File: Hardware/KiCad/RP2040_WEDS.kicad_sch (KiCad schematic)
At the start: 75 parts, among them J1 Barrel_Jack_Switch_Pin3Ring, J2 Conn_01x02_Male, J3 I2C Soil Header, J4 LiPo Batt, J5 Analog Soil Header, J6 USB Header, J7 Conn_02x05_Odd_Even, J8 SMA-J-P-H-RA-TH1, Q1 Q_PMOS_DGS, Q2 Q_PMOS_DGS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

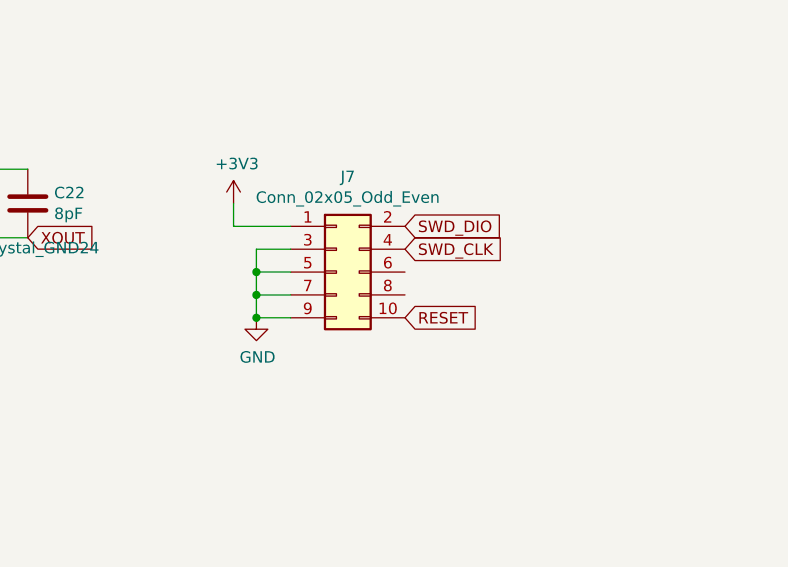
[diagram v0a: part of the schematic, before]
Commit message: added thermal relief to fill zones
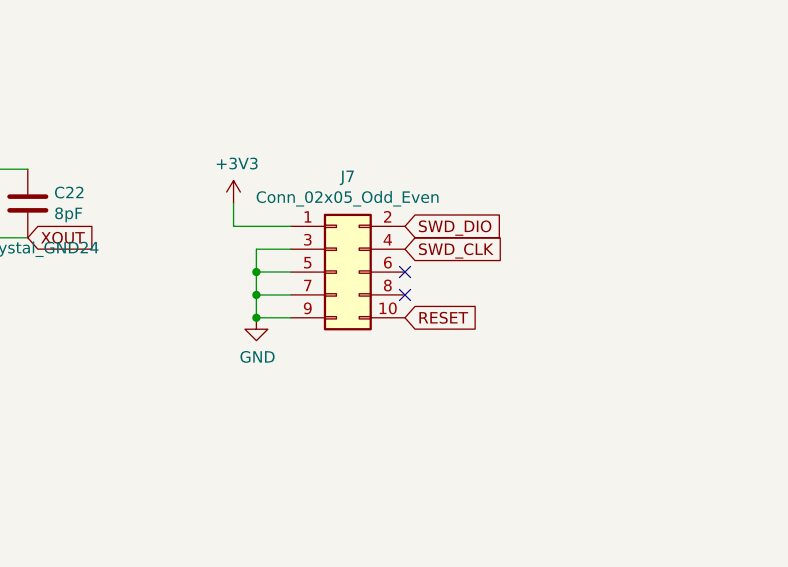
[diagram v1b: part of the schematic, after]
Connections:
- no-connect marks 41 -> 43
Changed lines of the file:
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@@
   (no_connect (at 35.56 149.86))
   (no_connect (at 81.28 134.62))
+  (no_connect (at 266.7 153.67))
+  (no_connect (at 266.7 151.13))
   (no_connect (at 228.6 77.47))
   (no_connect (at 223.52 77.47))

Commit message: changed the size of headers form 1.27 to 2.54mm
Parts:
- J2: footprint Connector_PinHeader_1.27mm:PinHeader_1x02_P1.27mm_Vertical -> Connector_PinSocket_2.54mm:PinSocket_1x02_P2.54mm_Vertical
- J3: footprint Connector_PinHeader_1.27mm:PinHeader_1x04_P1.27mm_Vertical -> Connector_PinHeader_2.54mm:PinHeader_1x04_P2.54mm_Horizontal
- J4: footprint Connector_PinHeader_1.27mm:PinHeader_2x01_P1.27mm_Vertical -> Connector_PinHeader_2.54mm:PinHeader_2x01_P2.54mm_Vertical
- J5: footprint Connector_PinHeader_1.27mm:PinHeader_1x03_P1.27mm_Vertical -> Connector_PinHeader_2.54mm:PinHeader_1x03_P2.54mm_Horizontal
- J6: footprint Connector_PinHeader_1.27mm:PinHeader_1x04_P1.27mm_Vertical -> Connector_PinHeader_2.54mm:PinHeader_1x04_P2.54mm_Vertical
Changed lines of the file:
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@@
       (effects (font (size 1.27 1.27)) (justify left))
     )
-    (property "Footprint" "Connector_PinHeader_1.27mm:PinHeader_2x01_P1.27mm_Vertical" (id 2) (at 106.68 54.61 0)
+    (property "Footprint" "Connector_PinHeader_2.54mm:PinHeader_2x01_P2.54mm_Vertical" (id 2) (at 106.68 54.61 0)
       (effects (font (size 1.27 1.27)) hide)
     )
@@
     (property "Reference" "J5" (id 0) (at 138.6332 122.4026 0))
     (property "Value" "Analog Soil Header" (id 1) (at 138.6332 124.714 0))
-    (property "Footprint" "Connector_PinHeader_1.27mm:PinHeader_1x03_P1.27mm_Vertical" (id 2) (at 135.89 129.54 0)
+    (property "Footprint" "Connector_PinHeader_2.54mm:PinHeader_1x03_P2.54mm_Horizontal" (id 2) (at 135.89 129.54 0)
       (effects (font (size 1.27 1.27)) hide)
     )
@@
     (property "Reference" "J3" (id 0) (at 108.1532 122.4026 0))
     (property "Value" "I2C Soil Header" (id 1) (at 108.1532 124.714 0))
-    (property "Footprint" "Connector_PinHeader_1.27mm:PinHeader_1x04_P1.27mm_Vertical" (id 2) (at 105.41 129.54 0)
+    (property "Footprint" "Connector_PinHeader_2.54mm:PinHeader_1x04_P2.54mm_Horizontal" (id 2) (at 105.41 129.54 0)
       (effects (font (size 1.27 1.27)) hide)
     )
@@
     (property "Reference" "J2" (id 0) (at 93.345 168.944 0))
     (property "Value" "Conn_01x02_Male" (id 1) (at 87.63 177.8 0))
-    (property "Footprint" "Connector_PinHeader_1.27mm:PinHeader_1x02_P1.27mm_Vertical" (id 2) (at 92.71 172.72 0)
+    (property "Footprint" "Connector_PinSocket_2.54mm:PinSocket_1x02_P2.54mm_Vertical" (id 2) (at 92.71 172.72 0)
       (effects (font (size 1.27 1.27)) hide)
     )
@@
     (property "Reference" "J6" (id 0) (at 169.545 121.92 0))
     (property "Value" "USB Header" (id 1) (at 169.545 124.46 0))
-    (property "Footprint" "Connector_PinHeader_1.27mm:PinHeader_1x04_P1.27mm_Vertical" (id 2) (at 168.91 129.54 0)
+    (property "Footprint" "Connector_PinHeader_2.54mm:PinHeader_1x04_P2.54mm_Vertical" (id 2) (at 168.91 129.54 0)
       (effects (font (size 1.27 1.27)) hide)
     )
@@
     )
     (path "/87f53324-fd34-468e-b98f-06d9b31382af"
-      (reference "J2") (unit 1) (value "Conn_01x02_Male") (footprint "Connector_PinHeader_1.27mm:PinHeader_1x02_P1.27mm_Vertical")
+      (reference "J2") (unit 1) (value "Conn_01x02_Male") (footprint "Connector_PinSocket_2.54mm:PinSocket_1x02_P2.54mm_Vertical")
     )
     (path "/00000000-0000-0000-0000-0000625e3cae"
-      (reference "J3") (unit 1) (value "I2C Soil Header") (footprint "Connector_PinHeader_1.27mm:PinHeader_1x04_P1.27mm_Vertical")
+      (reference "J3") (unit 1) (value "I2C Soil Header") (footprint "Connector_PinHeader_2.54mm:PinHeader_1x04_P2.54mm_Horizontal")
     )
     (path "/00000000-0000-0000-0000-00006209bd4a"
-      (reference "J4") (unit 1) (value "LiPo Batt") (footprint "Connector_PinHeader_1.27mm:PinHeader_2x01_P1.27mm_Vertical")
+      (reference "J4") (unit 1) (value "LiPo Batt") (footprint "Connector_PinHeader_2.54mm:PinHeader_2x01_P2.54mm_Vertical")
     )
     (path "/00000000-0000-0000-0000-0000625a9016"
-      (reference "J5") (unit 1) (value "Analog Soil Header") (footprint "Connector_PinHeader_1.27mm:PinHeader_1x03_P1.27mm_Vertical")
+      (reference "J5") (unit 1) (value "Analog Soil Header") (footprint "Connector_PinHeader_2.54mm:PinHeader_1x03_P2.54mm_Horizontal")
     )
     (path "/dc005aba-36e3-4558-88a0-257925ac0539"
-      (reference "J6") (unit 1) (value "USB Header") (footprint "Connector_PinHeader_1.27mm:PinHeader_1x04_P1.27mm_Vertical")
+      (reference "J6") (unit 1) (value "USB Header") (footprint "Connector_PinHeader_2.54mm:PinHeader_1x04_P2.54mm_Vertical")
     )
     (path "/00000000-0000-0000-0000-0000621ac2f6"
